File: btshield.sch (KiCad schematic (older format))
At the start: 15 parts, among them SW1 SW_PUSH, SW2 SW_PUSH, SW3 SW_PUSH, SW4 SW_PUSH, SW5 SW_PUSH, U1 HC-10

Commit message: shield and schematic w/o missing pieces
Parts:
- removed C1: 0.1uF, Capacitors_ThroughHole:C_Disc_D3_P2.5, symbol C-RESCUE-$btshield
- added C?: C, symbol C
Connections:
- wire segments 50 -> 49
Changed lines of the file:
@@
 EESchema Schematic File Version 2
-LIBS:$btshield-rescue
 LIBS:power
 LIBS:device
@@
 LIBS:valves
 LIBS:btshield
-LIBS:arduino_shieldsNCL
-LIBS:$btshield-cache
+LIBS:Arduino_As_Uno-cache
 EELAYER 25 0
 EELAYER END
@@
 $EndComp
 $Comp
-L C-RESCUE-$btshield C1
-U 1 1 55B1AA1D
-P 4300 3950
-F 0 "C1" H 4300 4050 40  0000 L CNN
-F 1 "0.1uF" H 4306 3865 40  0000 L CNN
-F 2 "Capacitors_ThroughHole:C_Disc_D3_P2.5" H 4338 3800 30  0001 C CNN
-F 3 "~" H 4300 3950 60  0000 C CNN
-	1    4300 3950
-	1    0    0    -1
-$EndComp
-$Comp
-L GND-RESCUE-$btshield #GND01
-U 1 1 55B1AA3A
-P 4300 4300
-F 0 "#GND01" H 4300 4300 30  0001 C CNN
-F 1 "GND" H 4300 4230 30  0001 C CNN
-F 2 "" H 4300 4300 60  0000 C CNN
-F 3 "" H 4300 4300 60  0000 C CNN
-	1    4300 4300
-	1    0    0    -1
-$EndComp
-$Comp
-L GND-RESCUE-$btshield #GND02
-U 1 1 55B1AAEB
-P 4950 4500
-F 0 "#GND02" H 4950 4500 30  0001 C CNN
-F 1 "GND" H 4950 4430 30  0001 C CNN
-F 2 "" H 4950 4500 60  0000 C CNN
-F 3 "" H 4950 4500 60  0000 C CNN
-	1    4950 4500
-	1    0    0    -1
-$EndComp
-$Comp
-L GND-RESCUE-$btshield #GND03
-U 1 1 55B1ABBE
-P 6550 5600
-F 0 "#GND03" H 6550 5600 30  0001 C CNN
-F 1 "GND" H 6550 5530 30  0001 C CNN
-F 2 "" H 6550 5600 60  0000 C CNN
-F 3 "" H 6550 5600 60  0000 C CNN
-	1    6550 5600
-	1    0    0    -1
-$EndComp
-$Comp
 L R-RESCUE-$btshield R6
 U 1 1 55B1AC33
@@
 $EndComp
 Wire Wire Line
-	4300 4150 4300 4300
-Wire Wire Line
 	4300 3750 5150 3750
 Wire Wire Line
-	4300 3450 4300 3750
+	4300 3450 4300 3850
 Wire Wire Line
 	5150 3950 4950 3950
 Wire Wire Line
-	4950 3950 4950 4500
+	4950 3950 4950 4750
 Wire Wire Line
 	5150 4050 4950 4050
@@
 	0    1    1    0
 $EndComp
+$Comp
+L C C?
+U 1 1 55BA627D
+P 4300 4000
+F 0 "C?" H 4325 4100 50  0000 L CNN
+F 1 "C" H 4325 3900 50  0000 L CNN
+F 2 "" H 4338 3850 30  0000 C CNN
+F 3 "" H 4300 4000 60  0000 C CNN
+	1    4300 4000
+	1    0    0    -1
+$EndComp
+$Comp
+L GND #PWR?
+U 1 1 55BA62D8
+P 4300 4150
+F 0 "#PWR?" H 4300 3900 50  0001 C CNN
+F 1 "GND" H 4300 4000 50  0000 C CNN
+F 2 "" H 4300 4150 60  0000 C CNN
+F 3 "" H 4300 4150 60  0000 C CNN
+	1    4300 4150
+	1    0    0    -1
+$EndComp
+Connection ~ 4300 3750
+$Comp
+L GND #PWR?
+U 1 1 55BA65BE
+P 4950 4750
+F 0 "#PWR?" H 4950 4500 50  0001 C CNN
+F 1 "GND" H 4950 4600 50  0000 C CNN
+F 2 "" H 4950 4750 60  0000 C CNN
+F 3 "" H 4950 4750 60  0000 C CNN
+	1    4950 4750
+	1    0    0    -1
+$EndComp
+$Comp
+L GND #PWR?
+U 1 1 55BA68D7
+P 6550 5600
+F 0 "#PWR?" H 6550 5350 50  0001 C CNN
+F 1 "GND" H 6550 5450 50  0000 C CNN
+F 2 "" H 6550 5600 60  0000 C CNN
+F 3 "" H 6550 5600 60  0000 C CNN
+	1    6550 5600
+	1    0    0    -1
+$EndComp
 $EndSCHEMATC

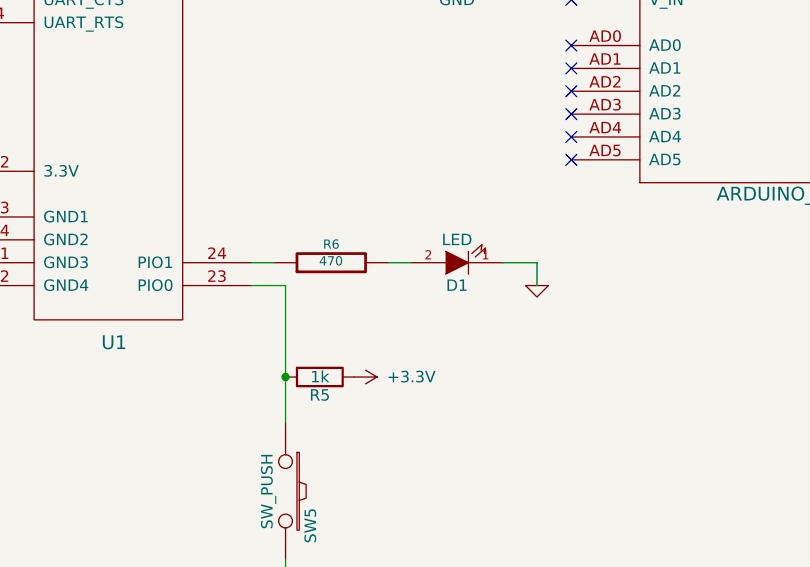
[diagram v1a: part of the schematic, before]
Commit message: fixed broken components (hopefully)
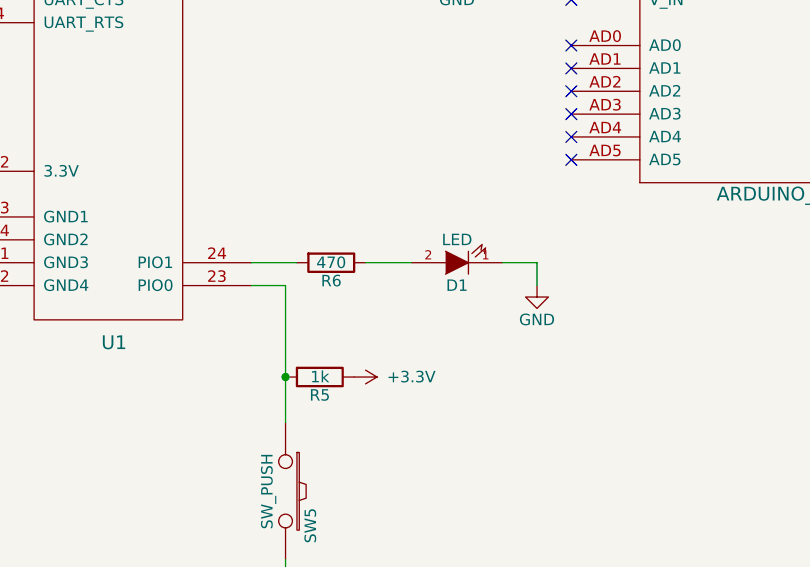
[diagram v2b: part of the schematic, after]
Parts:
- removed R6: 470, Resistors_ThroughHole:Resistor_Horizontal_RM10mm, symbol R-RESCUE-$btshield
- added R6: 470, symbol R
- C1: renamed from C?; footprint (none) -> Capacitors_ThroughHole:C_Disc_D3_P2.5
- D1: footprint LED-5MM -> LEDs:LED-5MM
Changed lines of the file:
@@
 LIBS:btshield
 LIBS:Arduino_As_Uno-cache
+LIBS:btshield-cache
 EELAYER 25 0
 EELAYER END
@@
 $EndComp
 $Comp
-L R-RESCUE-$btshield R6
-U 1 1 55B1AC33
-P 6750 4150
-F 0 "R6" V 6830 4150 40  0000 C CNN
-F 1 "470" V 6757 4151 40  0000 C CNN
-F 2 "Resistors_ThroughHole:Resistor_Horizontal_RM10mm" V 6680 4150 30  0001 C CNN
-F 3 "~" H 6750 4150 30  0000 C CNN
-	1    6750 4150
-	0    -1   -1   0
-$EndComp
-$Comp
-L GND-RESCUE-$btshield #GND04
-U 1 1 55B1AC65
-P 7650 4250
-F 0 "#GND04" H 7650 4250 30  0001 C CNN
-F 1 "GND" H 7650 4180 30  0001 C CNN
-F 2 "" H 7650 4250 60  0000 C CNN
-F 3 "" H 7650 4250 60  0000 C CNN
-	1    7650 4250
-	1    0    0    -1
-$EndComp
-$Comp
 L ARDUINO_SHIELD SHIELD1
 U 1 1 55B52CD4
@@
 $EndComp
 $Comp
-L +3.3V #PWR05
+L +3.3V #PWR01
 U 1 1 55B58087
 P 7450 2500
-F 0 "#PWR05" H 7450 2350 50  0001 C CNN
+F 0 "#PWR01" H 7450 2350 50  0001 C CNN
 F 1 "+3.3V" H 7450 2640 50  0000 C CNN
 F 2 "" H 7450 2500 60  0000 C CNN
@@
 $EndComp
 $Comp
-L +5V #PWR06
+L +5V #PWR02
 U 1 1 55B58201
 P 7300 2700
-F 0 "#PWR06" H 7300 2550 50  0001 C CNN
+F 0 "#PWR02" H 7300 2550 50  0001 C CNN
 F 1 "+5V" H 7300 2840 50  0000 C CNN
 F 2 "" H 7300 2700 60  0000 C CNN
@@
 $EndComp
 $Comp
-L GND #PWR07
+L GND #PWR03
 U 1 1 55B58353
 P 7300 2850
-F 0 "#PWR07" H 7300 2600 50  0001 C CNN
+F 0 "#PWR03" H 7300 2600 50  0001 C CNN
 F 1 "GND" H 7300 2700 50  0000 C CNN
 F 2 "" H 7300 2850 60  0000 C CNN
@@
 NoConn ~ 7800 3700
 $Comp
-L +3.3V #PWR08
+L +3.3V #PWR04
 U 1 1 55B5906D
 P 4300 3450
-F 0 "#PWR08" H 4300 3300 50  0001 C CNN
+F 0 "#PWR04" H 4300 3300 50  0001 C CNN
 F 1 "+3.3V" H 4300 3590 50  0000 C CNN
 F 2 "" H 4300 3450 60  0000 C CNN
@@
 $EndComp
 $Comp
-L +3.3V #PWR09
+L +3.3V #PWR05
 U 1 1 55B592BB
 P 6850 4650
-F 0 "#PWR09" H 6850 4500 50  0001 C CNN
+F 0 "#PWR05" H 6850 4500 50  0001 C CNN
 F 1 "+3.3V" V 6850 4900 50  0000 C CNN
 F 2 "" H 6850 4650 60  0000 C CNN
@@
 $EndSheet
 $Comp
-L +3.3V #PWR010
+L +3.3V #PWR06
 U 1 1 55B660EF
 P 5650 1300
-F 0 "#PWR010" H 5650 1150 50  0001 C CNN
+F 0 "#PWR06" H 5650 1150 50  0001 C CNN
 F 1 "+3.3V" V 5650 1550 50  0000 C CNN
 F 2 "" H 5650 1300 60  0000 C CNN
@@
 $EndComp
 $Comp
-L +5V #PWR011
+L +5V #PWR07
 U 1 1 55B66932
 P 6300 1300
-F 0 "#PWR011" H 6300 1150 50  0001 C CNN
+F 0 "#PWR07" H 6300 1150 50  0001 C CNN
 F 1 "+5V" V 6300 1500 50  0000 C CNN
 F 2 "" H 6300 1300 60  0000 C CNN
@@
 $EndComp
 $Comp
-L GND #PWR012
+L GND #PWR08
 U 1 1 55B6D517
 P 2650 1400
-F 0 "#PWR012" H 2650 1150 50  0001 C CNN
+F 0 "#PWR08" H 2650 1150 50  0001 C CNN
 F 1 "GND" H 2650 1250 50  0000 C CNN
 F 2 "" H 2650 1400 60  0000 C CNN
@@
 	6550 4250 6550 4850
 Wire Wire Line
-	6400 4150 6500 4150
-Wire Wire Line
 	7450 2600 7800 2600
 Wire Wire Line
@@
 Connection ~ 2250 1100
 $Comp
-L +5V #PWR013
+L +5V #PWR09
 U 1 1 55B6E084
 P 1250 950
-F 0 "#PWR013" H 1250 800 50  0001 C CNN
+F 0 "#PWR09" H 1250 800 50  0001 C CNN
 F 1 "+5V" H 1250 1090 50  0000 C CNN
 F 2 "" H 1250 950 60  0000 C CNN
@@
 $EndComp
 $Comp
-L GND #PWR014
+L GND #PWR010
 U 1 1 55B73A27
 P 2650 2400
-F 0 "#PWR014" H 2650 2150 50  0001 C CNN
+F 0 "#PWR010" H 2650 2150 50  0001 C CNN
 F 1 "GND" H 2650 2250 50  0000 C CNN
 F 2 "" H 2650 2400 60  0000 C CNN
@@
 Connection ~ 2250 2100
 $Comp
-L +5V #PWR015
+L +5V #PWR011
 U 1 1 55B73A30
 P 1250 1950
-F 0 "#PWR015" H 1250 1800 50  0001 C CNN
+F 0 "#PWR011" H 1250 1800 50  0001 C CNN
 F 1 "+5V" H 1250 2090 50  0000 C CNN
 F 2 "" H 1250 1950 60  0000 C CNN
@@
 $EndComp
 $Comp
-L GND #PWR016
+L GND #PWR012
 U 1 1 55B74061
 P 2650 3400
-F 0 "#PWR016" H 2650 3150 50  0001 C CNN
+F 0 "#PWR012" H 2650 3150 50  0001 C CNN
 F 1 "GND" H 2650 3250 50  0000 C CNN
 F 2 "" H 2650 3400 60  0000 C CNN
@@
 Connection ~ 2250 3100
 $Comp
-L +5V #PWR017
+L +5V #PWR013
 U 1 1 55B7406A
 P 1250 2950
-F 0 "#PWR017" H 1250 2800 50  0001 C CNN
+F 0 "#PWR013" H 1250 2800 50  0001 C CNN
 F 1 "+5V" H 1250 3090 50  0000 C CNN
 F 2 "" H 1250 2950 60  0000 C CNN
@@
 $EndComp
 $Comp
-L GND #PWR018
+L GND #PWR014
 U 1 1 55B7412D
 P 2650 4300
-F 0 "#PWR018" H 2650 4050 50  0001 C CNN
+F 0 "#PWR014" H 2650 4050 50  0001 C CNN
 F 1 "GND" H 2650 4150 50  0000 C CNN
 F 2 "" H 2650 4300 60  0000 C CNN
@@
 Connection ~ 2250 4000
 $Comp
-L +5V #PWR019
+L +5V #PWR015
 U 1 1 55B74136
 P 1250 3850
-F 0 "#PWR019" H 1250 3700 50  0001 C CNN
+F 0 "#PWR015" H 1250 3700 50  0001 C CNN
 F 1 "+5V" H 1250 3990 50  0000 C CNN
 F 2 "" H 1250 3850 60  0000 C CNN
@@
 F 0 "D1" H 7300 4250 50  0000 C CNN
 F 1 "LED" H 7300 4050 50  0000 C CNN
-F 2 "LED-5MM" H 7300 4150 60  0001 C CNN
+F 2 "LEDs:LED-5MM" H 7300 4150 60  0001 C CNN
 F 3 "" H 7300 4150 60  0000 C CNN
 	1    7300 4150
 	-1   0    0    1
 $EndComp
-Wire Wire Line
-	7000 4150 7100 4150
-Wire Wire Line
-	7500 4150 7650 4150
 Wire Wire Line
 	7650 4150 7650 4250
@@
 $EndComp
 $Comp
-L C C?
+L C C1
 U 1 1 55BA627D
 P 4300 4000
-F 0 "C?" H 4325 4100 50  0000 L CNN
+F 0 "C1" H 4325 4100 50  0000 L CNN
 F 1 "C" H 4325 3900 50  0000 L CNN
-F 2 "" H 4338 3850 30  0000 C CNN
+F 2 "Capacitors_ThroughHole:C_Disc_D3_P2.5" H 4338 3850 30  0001 C CNN
 F 3 "" H 4300 4000 60  0000 C CNN
 	1    4300 4000
@@
 $EndComp
 $Comp
-L GND #PWR?
+L GND #PWR016
 U 1 1 55BA62D8
 P 4300 4150
-F 0 "#PWR?" H 4300 3900 50  0001 C CNN
+F 0 "#PWR016" H 4300 3900 50  0001 C CNN
 F 1 "GND" H 4300 4000 50  0000 C CNN
 F 2 "" H 4300 4150 60  0000 C CNN
@@
 Connection ~ 4300 3750
 $Comp
-L GND #PWR?
+L GND #PWR017
 U 1 1 55BA65BE
 P 4950 4750
-F 0 "#PWR?" H 4950 4500 50  0001 C CNN
+F 0 "#PWR017" H 4950 4500 50  0001 C CNN
 F 1 "GND" H 4950 4600 50  0000 C CNN
 F 2 "" H 4950 4750 60  0000 C CNN
@@
 $EndComp
 $Comp
-L GND #PWR?
+L GND #PWR018
 U 1 1 55BA68D7
 P 6550 5600
-F 0 "#PWR?" H 6550 5350 50  0001 C CNN
+F 0 "#PWR018" H 6550 5350 50  0001 C CNN
 F 1 "GND" H 6550 5450 50  0000 C CNN
 F 2 "" H 6550 5600 60  0000 C CNN
@@
 	1    0    0    -1
 $EndComp
+$Comp
+L R R6
+U 1 1 55BAB88D
+P 6750 4150
+F 0 "R6" V 6830 4150 50  0000 C CNN
+F 1 "470" V 6750 4150 50  0000 C CNN
+F 2 "" V 6680 4150 30  0001 C CNN
+F 3 "" H 6750 4150 30  0000 C CNN
+	1    6750 4150
+	0    1    1    0
+$EndComp
+$Comp
+L GND #PWR019
+U 1 1 55BB22C6
+P 7650 4250
+F 0 "#PWR019" H 7650 4000 50  0001 C CNN
+F 1 "GND" H 7650 4100 50  0000 C CNN
+F 2 "" H 7650 4250 60  0000 C CNN
+F 3 "" H 7650 4250 60  0000 C CNN
+	1    7650 4250
+	1    0    0    -1
+$EndComp
+Wire Wire Line
+	6400 4150 6600 4150
+Wire Wire Line
+	6900 4150 7100 4150
+Wire Wire Line
+	7500 4150 7650 4150
 $EndSCHEMATC
